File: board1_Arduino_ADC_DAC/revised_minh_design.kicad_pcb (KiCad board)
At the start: 4 copper layers, 96 x 43.9 mm, 40 parts, among them J1 Conn_01x03_Male, J2 Conn_02x08_Odd_Even, J3 Conn_02x08_Odd_Even, J4 Conn_02x08_Odd_Even, J5 Conn_01x02_Male, U1 ESP32-DevKit-C, U2 LM7805_TO220, U3 MCP1754S-3302xCB, U4 MCP1825S-3.3V, U5 MCP1501-33xSN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

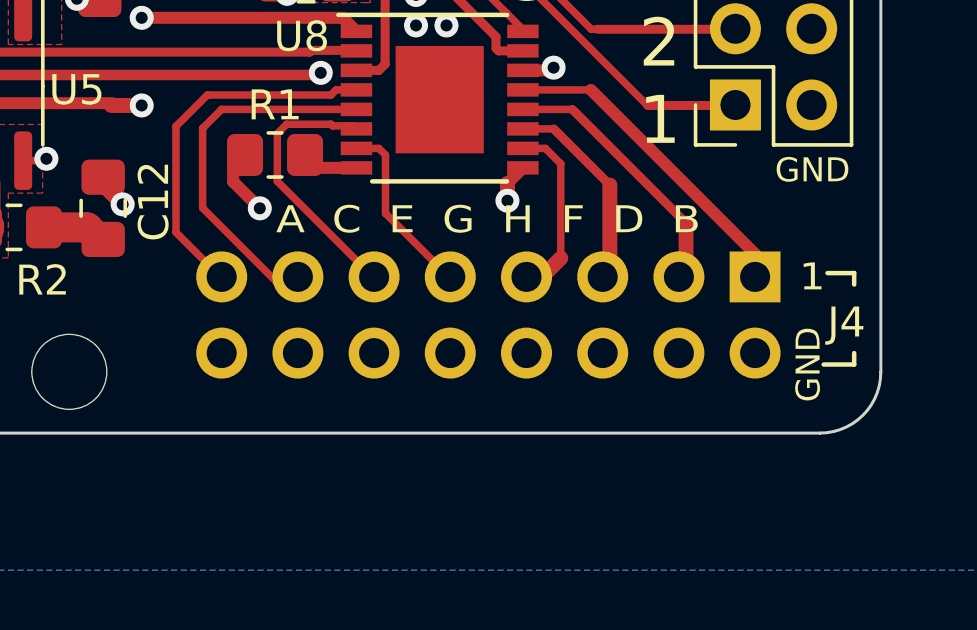
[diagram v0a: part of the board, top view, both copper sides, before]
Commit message: exported STEP file. Minor changes to schematics for better documentations
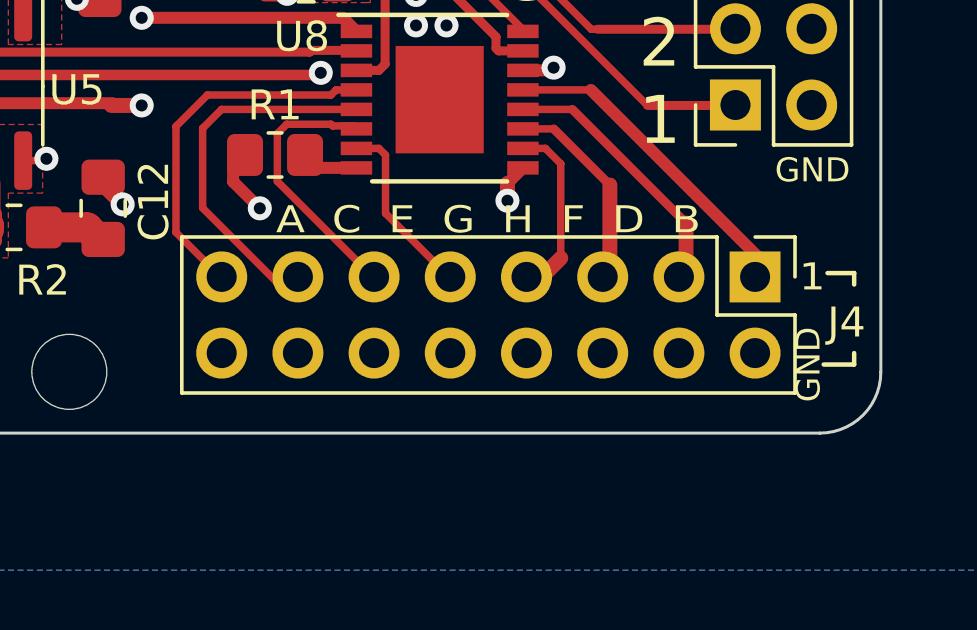
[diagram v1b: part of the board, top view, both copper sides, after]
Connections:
- net SI renamed PI
- net SO renamed PO
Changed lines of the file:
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@@
   (net 59 "~{DAC_CS}")
   (net 60 "SK")
-  (net 61 "SI")
-  (net 62 "SO")
+  (net 61 "PI")
+  (net 62 "PO")
   (net 63 "unconnected-(U1-Pad35)")
   (net 64 "unconnected-(U1-Pad36)")
@@
       (net 60 "SK") (pinfunction "SCK") (pintype "input"))
     (pad "15" smd roundrect locked (at 2.8625 0.325 180) (size 1.475 0.4) (layers "F.Cu" "F.Paste" "F.Mask") (roundrect_rratio 0.25)
-      (net 61 "SI") (pinfunction "SDI") (pintype "input"))
+      (net 61 "PI") (pinfunction "SDI") (pintype "input"))
     (pad "16" smd roundrect locked (at 2.8625 -0.325 180) (size 1.475 0.4) (layers "F.Cu" "F.Paste" "F.Mask") (roundrect_rratio 0.25)
-      (net 62 "SO") (pinfunction "SDO") (pintype "input"))
+      (net 62 "PO") (pinfunction "SDO") (pintype "input"))
     (pad "17" smd roundrect locked (at 2.8625 -0.975 180) (size 1.475 0.4) (layers "F.Cu" "F.Paste" "F.Mask") (roundrect_rratio 0.25)
       (net 54 "MDAT") (pinfunction "~{IRQ}/MDAT") (pintype "input"))
@@
       (net 60 "SK") (pinfunction "SCK") (pintype "input"))
     (pad "15" smd roundrect locked (at 2.8625 0.325 90) (size 1.475 0.4) (layers "F.Cu" "F.Paste" "F.Mask") (roundrect_rratio 0.25)
-      (net 61 "SI") (pinfunction "SDI") (pintype "input"))
+      (net 61 "PI") (pinfunction "SDI") (pintype "input"))
     (pad "16" smd roundrect locked (at 2.8625 -0.325 90) (size 1.475 0.4) (layers "F.Cu" "F.Paste" "F.Mask") (roundrect_rratio 0.25)
-      (net 62 "SO") (pinfunction "SDO") (pintype "input"))
+      (net 62 "PO") (pinfunction "SDO") (pintype "input"))
     (pad "17" smd roundrect locked (at 2.8625 -0.975 90) (size 1.475 0.4) (layers "F.Cu" "F.Paste" "F.Mask") (roundrect_rratio 0.25)
       (net 54 "MDAT") (pinfunction "~{IRQ}/MDAT") (pintype "input"))
@@
       (net 2 "Earth") (pinfunction "GND") (pintype "input"))
     (pad "15" smd rect locked (at 2.775 -1.625) (size 1.05 0.45) (layers "F.Cu" "F.Paste" "F.Mask")
-      (net 62 "SO") (pinfunction "D_{IN}") (pintype "input"))
+      (net 62 "PO") (pinfunction "D_{IN}") (pintype "input"))
     (pad "16" smd rect locked (at 2.775 -2.275) (size 1.05 0.45) (layers "F.Cu" "F.Paste" "F.Mask")
       (net 60 "SK") (pinfunction "SCLK") (pintype "input"))
@@
       (net 60 "SK") (pinfunction "14") (pintype "input"))
     (pad "32" thru_hole circle (at -12.186285 -17.528858 90) (size 1.6 1.6) (drill 1.2) (layers *.Cu *.Mask)
-      (net 61 "SI") (pinfunction "12") (pintype "input"))
+      (net 61 "PI") (pinfunction "12") (pintype "input"))
     (pad "33" thru_hole circle (at -12.192 -20.066 90) (size 1.6 1.6) (drill 1.2) (layers *.Cu *.Mask)
       (net 2 "Earth") (pinfunction "GND") (pintype "input"))
     (pad "34" thru_hole circle (at -12.192 -22.606 90) (size 1.6 1.6) (drill 1.2) (layers *.Cu *.Mask)
-      (net 62 "SO") (pinfunction "13") (pintype "input"))
+      (net 62 "PO") (pinfunction "13") (pintype "input"))
     (pad "35" thru_hole circle (at -12.192 -25.146 90) (size 1.6 1.6) (drill 1.2) (layers *.Cu *.Mask)
       (net 63 "unconnected-(U1-Pad35)") (pinfunction "D2") (pintype "input+no_connect"))
@@
     (property "Sheetname" "")
     (attr through_hole)
-    (fp_text reference "J4" (at -1.524 3.048 180) (layer "F.SilkS")
-      (effects (font (size 1 1) (thickness 0.15)))
-    )
-    (fp_text value "Conn_02x08_Odd_Even" (at -1.27 -20.55 90) (layer "B.Fab")
+    (fp_text reference "J4" (at -1.524 3.048) (layer "F.SilkS")
+      (effects (font (size 1 1) (thickness 0.15)))
+    )
+    (fp_text value "Conn_02x08_Odd_Even" (at -1.27 -20.55 270) (layer "B.Fab")
       (effects (font (size 1 1) (thickness 0.15)) (justify mirror))
     )
@@
       (effects (font (size 1 1) (thickness 0.15)) (justify mirror))
     )
-    (fp_line (start 1.33 1.33) (end 1.33 0) (layer "B.SilkS") (width 0.12))
-    (fp_line (start -3.87 1.33) (end -1.27 1.33) (layer "B.SilkS") (width 0.12))
-    (fp_line (start 1.33 -1.27) (end 1.33 -19.11) (layer "B.SilkS") (width 0.12))
-    (fp_line (start -3.87 1.33) (end -3.87 -19.11) (layer "B.SilkS") (width 0.12))
-    (fp_line (start 0 1.33) (end 1.33 1.33) (layer "B.SilkS") (width 0.12))
-    (fp_line (start -1.27 -1.27) (end 1.33 -1.27) (layer "B.SilkS") (width 0.12))
-    (fp_line (start -3.87 -19.11) (end 1.33 -19.11) (layer "B.SilkS") (width 0.12))
-    (fp_line (start -1.27 1.33) (end -1.27 -1.27) (layer "B.SilkS") (width 0.12))
+    (fp_line (start 1.33 1.33) (end 1.33 0) (layer "F.SilkS") (width 0.12))
+    (fp_line (start -3.87 1.33) (end -1.27 1.33) (layer "F.SilkS") (width 0.12))
+    (fp_line (start 1.33 -1.27) (end 1.33 -19.11) (layer "F.SilkS") (width 0.12))
+    (fp_line (start -3.87 1.33) (end -3.87 -19.11) (layer "F.SilkS") (width 0.12))
+    (fp_line (start 0 1.33) (end 1.33 1.33) (layer "F.SilkS") (width 0.12))
+    (fp_line (start -1.27 -1.27) (end 1.33 -1.27) (layer "F.SilkS") (width 0.12))
+    (fp_line (start -3.87 -19.11) (end 1.33 -19.11) (layer "F.SilkS") (width 0.12))
+    (fp_line (start -1.27 1.33) (end -1.27 -1.27) (layer "F.SilkS") (width 0.12))
     (fp_line (start -4.34 -19.55) (end -4.34 1.8) (layer "B.CrtYd") (width 0.05))
     (fp_line (start 1.76 -19.55) (end -4.34 -19.55) (layer "B.CrtYd") (width 0.05))
@@
       (net 73 "unconnected-(A1-Pad13)") (pinfunction "D10") (pintype "bidirectional"))
     (pad "14" thru_hole oval (at 0 -33.02 90) (size 1.6 1.6) (drill 1) (layers *.Cu *.Mask)
-      (net 61 "SI") (pinfunction "D11") (pintype "bidirectional"))
+      (net 61 "PI") (pinfunction "D11") (pintype "bidirectional"))
     (pad "15" thru_hole oval (at 0 -35.56 90) (size 1.6 1.6) (drill 1) (layers *.Cu *.Mask)
-      (net 62 "SO") (pinfunction "D12") (pintype "bidirectional"))
+      (net 62 "PO") (pinfunction "D12") (pintype "bidirectional"))
     (pad "16" thru_hole oval (at 15.24 -35.56 90) (size 1.6 1.6) (drill 1) (layers *.Cu *.Mask)
       (net 60 "SK") (pinfunction "D13") (pintype "bidirectional"))
